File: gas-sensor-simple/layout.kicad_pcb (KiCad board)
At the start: 2 copper layers, 91.4 x 99.1 mm, 43 parts, among them J1 2x5 pin, J2 2x5 socket, J3 2x5 pin, J4 1x2, J5 1x2, J6 1x2, J7 1x2, U1 MQ-8, U10 RG LED, U12 LM393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

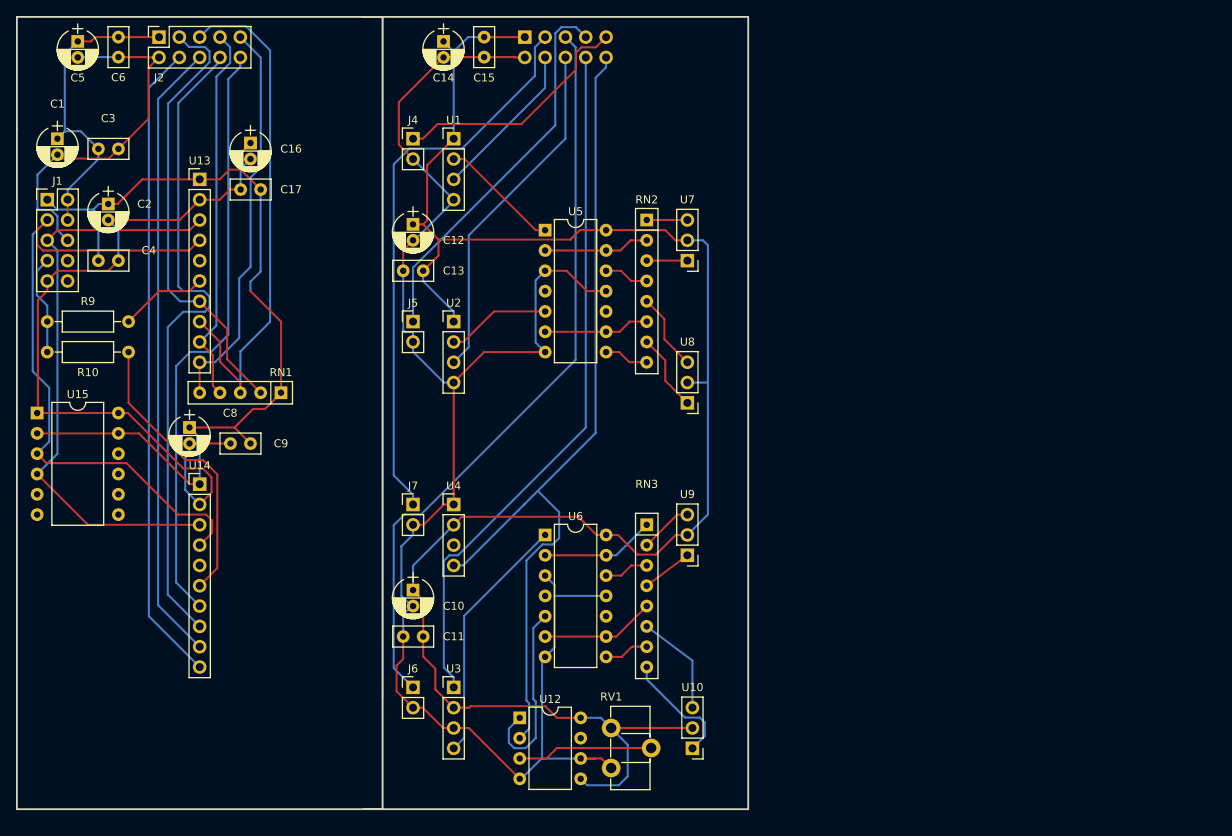
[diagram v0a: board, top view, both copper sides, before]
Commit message: Autorouted version 1 (gas-sensor-simple.kicad_pcb). Start work on version 2 layout (layout.kicad_pcb) moving RPi connector to top of digital board.
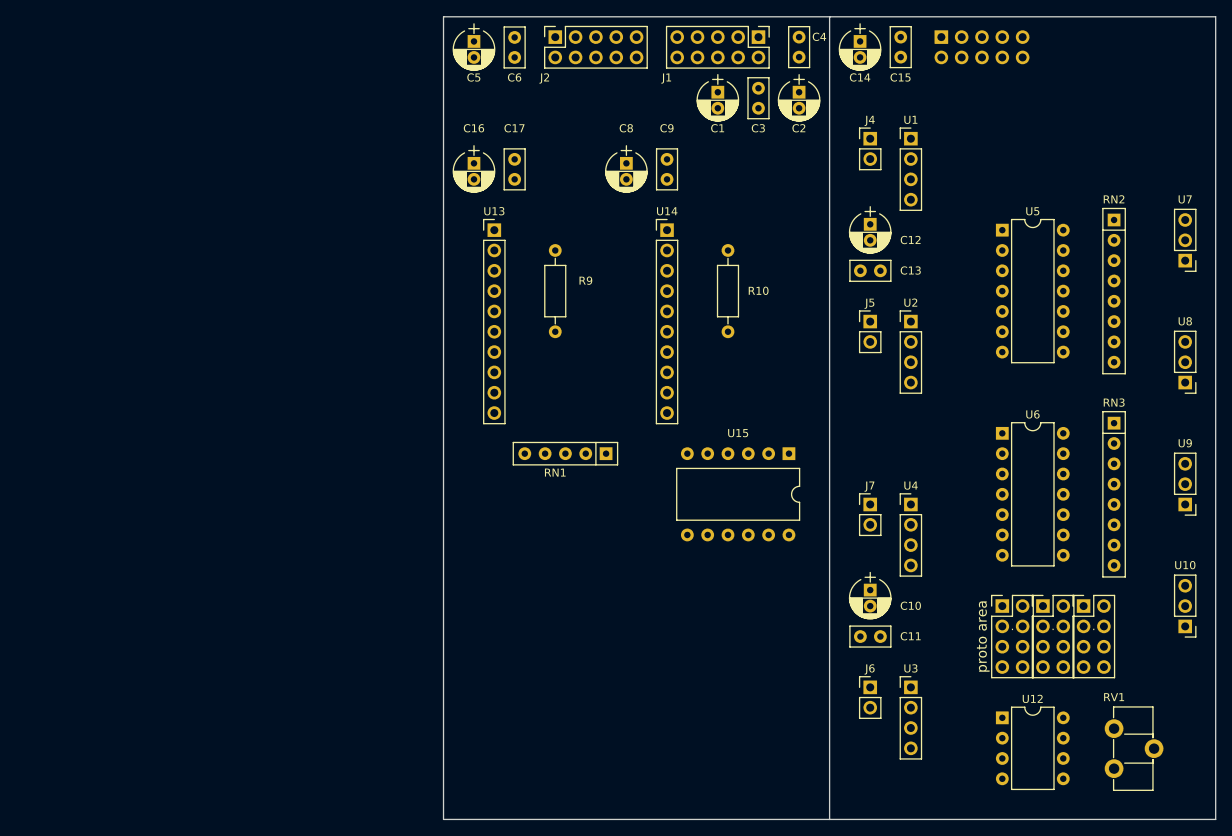
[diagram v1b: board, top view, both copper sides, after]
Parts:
- added .: ., Pin_Headers:Pin_Header_Straight_2x04_Pitch2.54mm, F.Cu at (226.1, 124.5)
- added .: ., Pin_Headers:Pin_Header_Straight_2x04_Pitch2.54mm, F.Cu at (231.1, 124.5)
- added .: ,, Pin_Headers:Pin_Header_Straight_2x04_Pitch2.54mm, F.Cu at (236.2, 124.5)
- J1: value 2x5 pin -> RPi
- J2: value 2x5 socket -> digital header
- J3: value 2x5 pin -> digital header
- RN3: value 4x180 -> 4x150
- moved U15 94.1 mm to (199.4, 105.4), turned to 270 degrees
- moved J1 91.2 mm to (195.6, 53.3), turned to 270 degrees
- moved C4 88.8 mm to (200.7, 55.8), turned to 90 degrees
- moved C2 87.5 mm to (200.7, 60.2)
- moved C1 82.8 mm to (190.5, 60.2)
- moved C3 80.2 mm to (195.6, 62.2), turned to 90 degrees
- moved R10 75.0 mm to (191.8, 90.2), turned to 90 degrees
- moved U14 66.5 mm to (184.2, 77.5)
- moved C8 63.8 mm to (179.1, 69.1)
- moved C9 63.8 mm to (184.2, 71.1), turned to 90 degrees
- moved U10 63.5 mm to (248.9, 127.0)
- moved RV1 62.9 mm to (240.0, 139.8)
- moved U9 62.6 mm to (248.9, 111.8)
- moved U8 62.3 mm to (248.9, 96.5)
- moved U7 62.2 mm to (248.9, 81.3)
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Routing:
- net VCC: track 269.4 -> 0.00 mm
- net GND: track 251.4 -> 0.00 mm
- net +3V3: track 114.9 -> 0.00 mm
- net Net-(J3-Pad10): track 107.2 -> 0.00 mm
- net GNDD: track 97.8 -> 0.00 mm
- net Net-(J3-Pad5): track 93.4 -> 0.00 mm
- net Net-(J3-Pad8): track 87.2 -> 0.00 mm
- net Net-(J1-Pad3): track 85.3 -> 0.00 mm
- net Net-(J2-Pad8): track 81.9 -> 0.00 mm
- net Net-(J2-Pad4): track 80.4 -> 0.00 mm
- net Net-(J2-Pad6): track 78.0 -> 0.00 mm
- net Net-(J2-Pad10): track 74.6 -> 0.00 mm
- net Net-(J1-Pad5): track 73.9 -> 0.00 mm
- net Net-(J3-Pad3): track 71.1 -> 0.00 mm
- net Net-(J2-Pad5): track 65.9 -> 0.00 mm
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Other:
- board size 91.4 x 99.1 mm -> 96.5 x 100.3 mm
- net class Default: trace_width 0.254 -> 0.381
- rule trace_min: 0.254 -> 0.381
- board text added: "proto area"
- board text removed: "1.0"
- board text removed: "2017-11-14"
- board text removed: "Analog gas sensor and digital interface"
- board text removed: "Gas Sensor v1"

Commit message: Updated layout.kicad_pcb with RPi connector moved, routed and cleaned up.
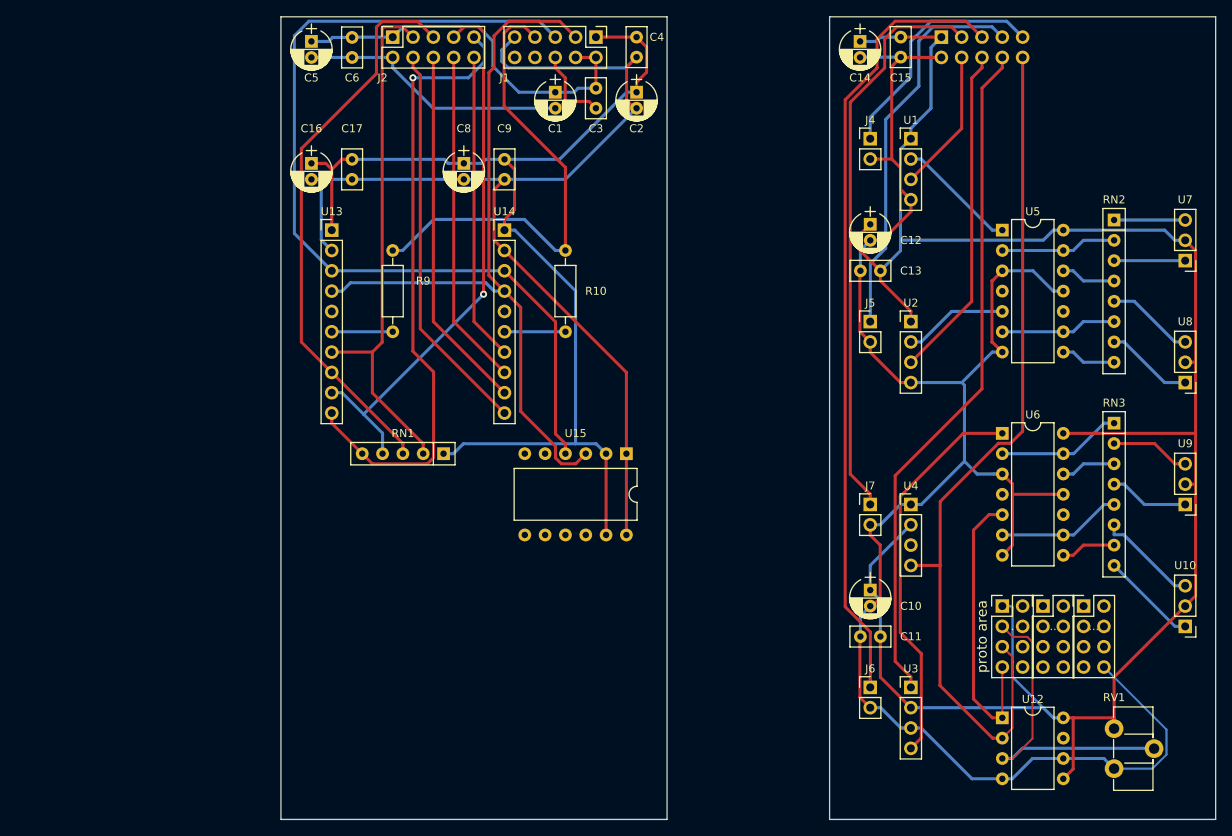
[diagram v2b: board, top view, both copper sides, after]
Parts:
- moved C16 20.3 mm to (139.7, 69.1)
- moved C3 20.3 mm to (175.3, 62.2)
- moved C5 20.3 mm to (139.7, 53.9)
- moved J1 20.3 mm to (175.3, 53.3)
- moved R10 20.3 mm to (171.4, 90.2)
- moved C1 20.3 mm to (170.2, 60.2)
- moved C17 20.3 mm to (144.8, 71.1)
- moved C2 20.3 mm to (180.3, 60.2)
- moved C4 20.3 mm to (180.3, 55.8)
- moved C6 20.3 mm to (144.8, 55.9)
- moved C8 20.3 mm to (158.8, 69.1)
- moved C9 20.3 mm to (163.8, 71.1)
- moved J2 20.3 mm to (149.9, 53.3)
- moved R9 20.3 mm to (149.9, 90.2)
- moved RN1 20.3 mm to (156.2, 105.4)
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- renumbered . to .., . to ...
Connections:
- . pad 1: (no net) -> VCC
- . pad 3: (no net) -> Net-(RV1-Pad2)
- . pad 5: (no net) -> Net-(J3-Pad10)
- . pad 7: (no net) -> Net-(U12-Pad1)
- ... pad 8: (no net) -> GND
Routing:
- net VCC: track 0.00 -> 304.4 mm
- net GND: track 0.00 -> 271.4 mm
- net +3V3: track 0.00 -> 138.5 mm
- net GNDD: track 0.00 -> 134.6 mm
- net Net-(J1-Pad5): track 0.00 -> 113.1 mm
- net Net-(J3-Pad10): track 0.00 -> 110.3 mm
- net Net-(J3-Pad5): track 0.00 -> 98.8 mm
- net Net-(J1-Pad3): track 0.00 -> 95.3 mm
- net Net-(J3-Pad8): track 0.00 -> 85.1 mm
- net Net-(J2-Pad9): track 0.00 -> 78.4 mm, vias 0 -> 1
- net Net-(J3-Pad3): track 0.00 -> 71.8 mm
- net Net-(J2-Pad5): track 0.00 -> 70.7 mm
- net Net-(J2-Pad7): track 0.00 -> 69.7 mm, vias 0 -> 1
- net Net-(J2-Pad3): track 0.00 -> 65.8 mm
- net Net-(J1-Pad7): track 0.00 -> 59.9 mm
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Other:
- board size 96.5 x 100.3 mm -> 116.8 x 100.3 mm
- net class Default: trace_width 0.381 -> 0.254
- rule trace_min: 0.381 -> 0.254
